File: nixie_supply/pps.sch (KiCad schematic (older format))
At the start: 5 parts

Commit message: minor cleanups
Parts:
- gave numbers to parts that had none: 3
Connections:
- net +5V: now also U5.2 (Enable); no longer U5.10 (Enable)
- net CLK_OUT: now also U5.14 (Q4); no longer U5.6 (Q4)
- net GND: now also U5.15 (Reset), U5.9 (CK); no longer U5.1 (CK), U5.7 (Reset)
- net at U4.6: now also U5.1 (CK); no longer U5.9 (CK)
- new net: U5.4 (Q2), U6.1
- new net: U5.10 (Enable), U5.5 (Q3), U6.2
- new net: U5.7 (Reset), U6.4
- new net: U6.3, U6.5, U6.6
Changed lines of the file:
@@
 $EndDescr
 $Comp
-L LM741 U?
+L LM741 U4
 U 1 1 5910E51A
 P 3200 2400
-F 0 "U?" H 3200 2650 50  0000 L CNN
+F 0 "U4" H 3200 2650 50  0000 L CNN
 F 1 "LM741" H 3200 2550 50  0000 L CNN
 F 2 "" H 3250 2450 50  0000 C CNN
@@
 $EndComp
 $Comp
-L 4518 U?
-U 2 1 5910E65E
+L 4518 U5
+U 1 1 5910E65E
 P 4650 2500
-F 0 "U?" H 4700 2950 50  0000 C CNN
+F 0 "U5" H 4700 2950 50  0000 C CNN
 F 1 "4518" H 4850 2150 50  0000 C CNN
 F 2 "" H 4650 2500 60  0001 C CNN
 F 3 "" H 4650 2500 60  0001 C CNN
-	2    4650 2500
-	1    0    0    -1
-$EndComp
-$Comp
-L 4518 U?
-U 1 1 5910E681
+	1    4650 2500
+	1    0    0    -1
+$EndComp
+$Comp
+L 4518 U5
+U 2 1 5910E681
 P 4650 4250
-F 0 "U?" H 4700 4700 50  0000 C CNN
+F 0 "U5" H 4700 4700 50  0000 C CNN
 F 1 "4518" H 4850 3900 50  0000 C CNN
 F 2 "" H 4650 4250 60  0001 C CNN
 F 3 "" H 4650 4250 60  0001 C CNN
-	1    4650 4250
-	1    0    0    -1
-$EndComp
-$Comp
-L 4011 U?
-U 4 1 5910E75D
+	2    4650 4250
+	1    0    0    -1
+$EndComp
+$Comp
+L 4011 U6
+U 1 1 5910E75D
 P 6200 2600
-F 0 "U?" H 6200 2650 50  0000 C CNN
+F 0 "U6" H 6200 2650 50  0000 C CNN
 F 1 "4011" H 6200 2550 50  0000 C CNN
 F 2 "" H 6200 2600 60  0001 C CNN
 F 3 "" H 6200 2600 60  0001 C CNN
-	4    6200 2600
-	1    0    0    -1
-$EndComp
-$Comp
-L 4011 U?
-U 1 1 5910E790
+	1    6200 2600
+	1    0    0    -1
+$EndComp
+$Comp
+L 4011 U6
+U 2 1 5910E790
 P 6200 3200
-F 0 "U?" H 6200 3250 50  0000 C CNN
+F 0 "U6" H 6200 3250 50  0000 C CNN
 F 1 "4011" H 6200 3150 50  0000 C CNN
 F 2 "" H 6200 3200 60  0001 C CNN
 F 3 "" H 6200 3200 60  0001 C CNN
-	1    6200 3200
+	2    6200 3200
 	1    0    0    -1
 $EndComp
@@
 NoConn ~ 5250 4100
 $Comp
-L +5V #PWR?
+L +5V #PWR035
 U 1 1 5910F1F9
 P 4050 2200
-F 0 "#PWR?" H 4050 2050 50  0001 C CNN
+F 0 "#PWR035" H 4050 2050 50  0001 C CNN
 F 1 "+5V" H 4050 2340 50  0000 C CNN
 F 2 "" H 4050 2200 50  0000 C CNN
@@
 $EndComp
 $Comp
-L +5V #PWR?
+L +5V #PWR036
 U 1 1 5910F217
 P 3100 2000
-F 0 "#PWR?" H 3100 1850 50  0001 C CNN
+F 0 "#PWR036" H 3100 1850 50  0001 C CNN
 F 1 "+5V" H 3100 2140 50  0000 C CNN
 F 2 "" H 3100 2000 50  0000 C CNN
@@
 $EndComp
 $Comp
-L GND #PWR?
+L GND #PWR037
 U 1 1 5910F235
 P 3100 2800
-F 0 "#PWR?" H 3100 2550 50  0001 C CNN
+F 0 "#PWR037" H 3100 2550 50  0001 C CNN
 F 1 "GND" H 3100 2650 50  0000 C CNN
 F 2 "" H 3100 2800 50  0000 C CNN
@@
 $EndComp
 $Comp
-L GND #PWR?
+L GND #PWR038
 U 1 1 5910F253
 P 3950 4400
-F 0 "#PWR?" H 3950 4150 50  0001 C CNN
+F 0 "#PWR038" H 3950 4150 50  0001 C CNN
 F 1 "GND" H 3950 4250 50  0000 C CNN
 F 2 "" H 3950 4400 50  0000 C CNN
@@
 Connection ~ 3950 4200
 $Comp
-L +5V #PWR?
+L +5V #PWR039
 U 1 1 5910F865
 P 2300 3300
-F 0 "#PWR?" H 2300 3150 50  0001 C CNN
+F 0 "#PWR039" H 2300 3150 50  0001 C CNN
 F 1 "+5V" H 2300 3440 50  0000 C CNN
 F 2 "" H 2300 3300 50  0000 C CNN
@@
 $EndComp
 $Comp
-L GND #PWR?
+L GND #PWR040
 U 1 1 5910F883
 P 2300 3600
-F 0 "#PWR?" H 2300 3350 50  0001 C CNN
+F 0 "#PWR040" H 2300 3350 50  0001 C CNN
 F 1 "GND" H 2300 3450 50  0000 C CNN
 F 2 "" H 2300 3600 50  0000 C CNN
@@
 $EndComp
 $Comp
-L VDD #PWR?
+L VDD #PWR041
 U 1 1 5910F8A1
 P 2550 3300
-F 0 "#PWR?" H 2550 3150 50  0001 C CNN
+F 0 "#PWR041" H 2550 3150 50  0001 C CNN
 F 1 "VDD" H 2550 3450 50  0000 C CNN
 F 2 "" H 2550 3300 50  0000 C CNN
@@
 $EndComp
 $Comp
-L VSS #PWR?
+L VSS #PWR042
 U 1 1 5910F8BF
 P 2550 3600
-F 0 "#PWR?" H 2550 3450 50  0001 C CNN
+F 0 "#PWR042" H 2550 3450 50  0001 C CNN
 F 1 "VSS" H 2550 3750 50  0000 C CNN
 F 2 "" H 2550 3600 50  0000 C CNN

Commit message: Footprint associations
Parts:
- U4: footprint (none) -> Housings_DIP:DIP-8_W7.62mm
- U5: footprint (none) -> Housings_DIP:DIP-16_W7.62mm
- U6: footprint (none) -> Housings_DIP:DIP-14_W7.62mm
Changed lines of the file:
@@
 F 0 "U4" H 3200 2650 50  0000 L CNN
 F 1 "LM741" H 3200 2550 50  0000 L CNN
-F 2 "" H 3250 2450 50  0000 C CNN
+F 2 "Housings_DIP:DIP-8_W7.62mm" H 3250 2450 50  0001 C CNN
 F 3 "" H 3350 2550 50  0000 C CNN
 	1    3200 2400
@@
 F 0 "U5" H 4700 2950 50  0000 C CNN
 F 1 "4518" H 4850 2150 50  0000 C CNN
-F 2 "" H 4650 2500 60  0001 C CNN
+F 2 "Housings_DIP:DIP-16_W7.62mm" H 4650 2500 60  0001 C CNN
 F 3 "" H 4650 2500 60  0001 C CNN
 	1    4650 2500
@@
 F 0 "U5" H 4700 4700 50  0000 C CNN
 F 1 "4518" H 4850 3900 50  0000 C CNN
-F 2 "" H 4650 4250 60  0001 C CNN
+F 2 "Housings_DIP:DIP-16_W7.62mm" H 4650 4250 60  0001 C CNN
 F 3 "" H 4650 4250 60  0001 C CNN
 	2    4650 4250
@@
 F 0 "U6" H 6200 2650 50  0000 C CNN
 F 1 "4011" H 6200 2550 50  0000 C CNN
-F 2 "" H 6200 2600 60  0001 C CNN
+F 2 "Housings_DIP:DIP-14_W7.62mm" H 6200 2600 60  0001 C CNN
 F 3 "" H 6200 2600 60  0001 C CNN
 	1    6200 2600
@@
 F 0 "U6" H 6200 3250 50  0000 C CNN
 F 1 "4011" H 6200 3150 50  0000 C CNN
-F 2 "" H 6200 3200 60  0001 C CNN
+F 2 "Housings_DIP:DIP-14_W7.62mm" H 6200 3200 60  0001 C CNN
 F 3 "" H 6200 3200 60  0001 C CNN
 	2    6200 3200

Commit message: Clock board layout
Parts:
- U4: symbol LM741 -> LM741-RESCUE-nixie_supply
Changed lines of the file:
@@
 EESchema Schematic File Version 2
+LIBS:nixie_supply-rescue
 LIBS:power
 LIBS:device
@@
 $EndDescr
 $Comp
-L LM741 U4
+L LM741-RESCUE-nixie_supply U4
 U 1 1 5910E51A
 P 3200 2400

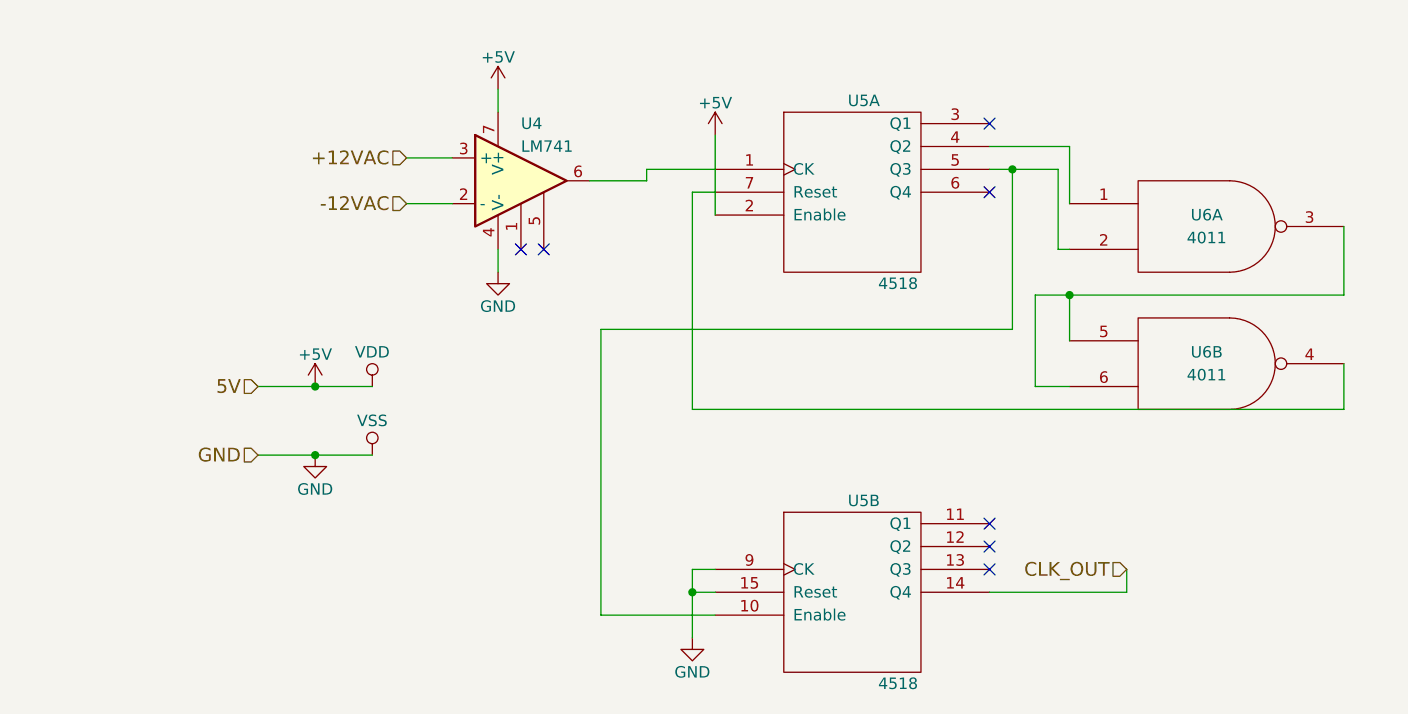
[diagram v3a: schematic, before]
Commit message: Supply board mk2: reduced time base noise, upped some clearances, added ground plane
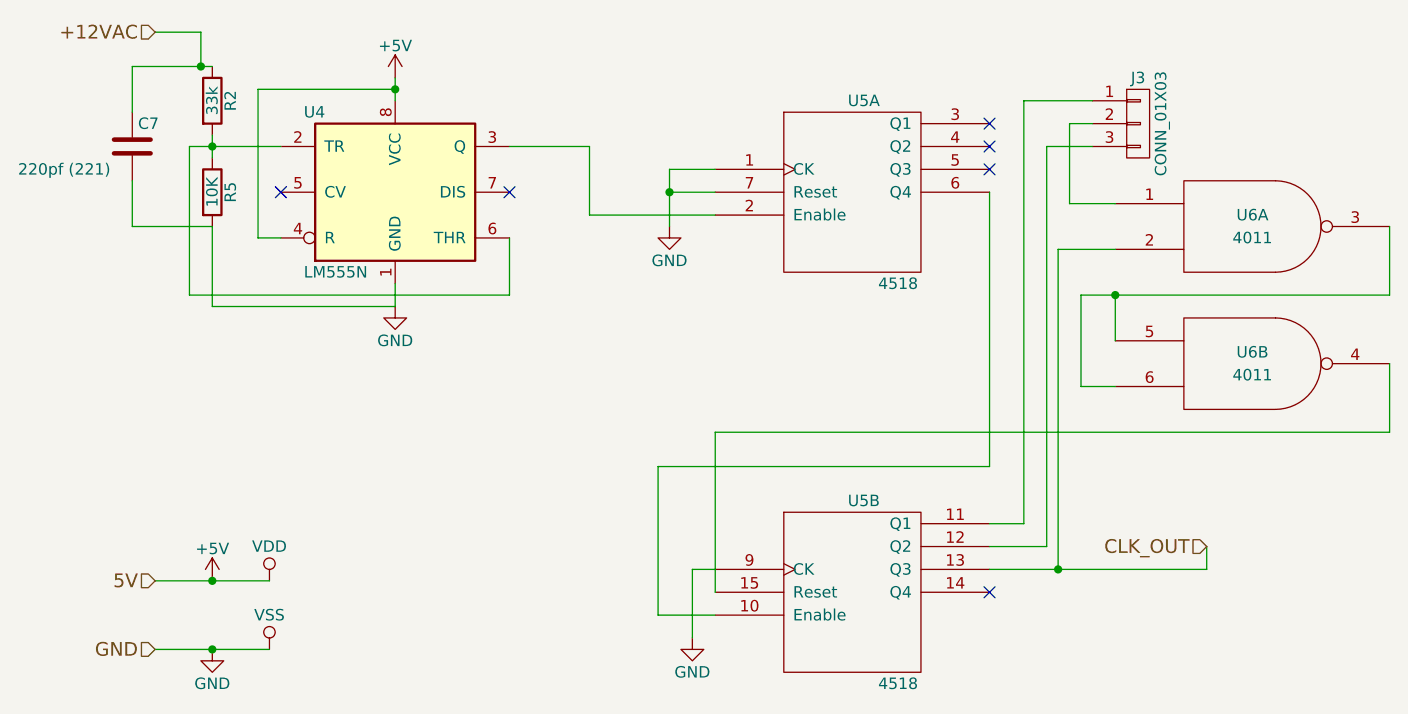
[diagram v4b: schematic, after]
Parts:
- removed U4: LM741, Housings_DIP:DIP-8_W7.62mm, symbol LM741-RESCUE-nixie_supply
- added C7: 220pf (221), Capacitors_THT:C_Disc_D10.0mm_W2.5mm_P5.00mm, symbol C
- added J3: CONN_01X03, Pin_Headers:Pin_Header_Straight_1x03_Pitch2.54mm, symbol CONN_01X03
- added R2: 33k, Resistors_THT:R_Axial_DIN0207_L6.3mm_D2.5mm_P10.16mm_Horizontal, symbol R
- added R5: 10K, Resistors_THT:R_Axial_DIN0207_L6.3mm_D2.5mm_P10.16mm_Horizontal, symbol R
- added U4: LM555N, Housings_DIP:DIP-8_W7.62mm, symbol LM555N
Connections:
- net +12VAC: now also C7.1, R2.1
- net +5V: now also U4.4 (R), U4.8 (VCC); no longer U5.2 (Enable)
- net CLK_OUT: now also U5.13 (Q3), U6.2; no longer U5.14 (Q4)
- net GND: now also U5.1 (CK), U5.7 (Reset), C7.2, R5.2, U4.1 (GND); no longer U5.15 (Reset)
- net at U5.4 (Q2): no longer U6.1
- net at U5.6 (Q4): now also U5.10 (Enable)
- net at U6.4: now also U5.15 (Reset); no longer U5.7 (Reset)
- net at U5.11 (Q1): now also J3.1 (P1)
- net at U5.12 (Q2): now also J3.3 (P3)
- new net: U4.3 (Q), U5.2 (Enable)
- new net: J3.2 (P2), U6.1
- new net: R2.2, R5.1, U4.2 (TR), U4.6 (THR)
- now unconnected: U5.5 (Q3)
- no-connect marks 7 -> 6
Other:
- moved on the sheet: U6A, U6B

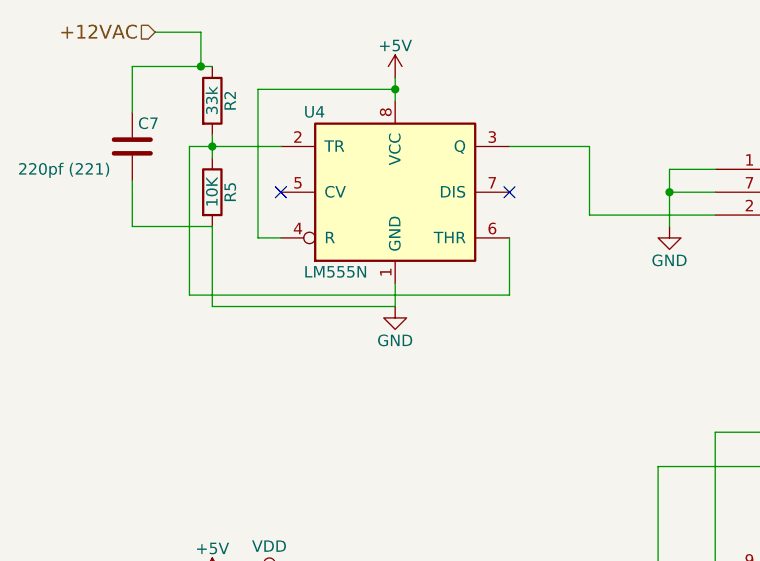
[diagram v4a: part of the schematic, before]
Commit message: Added more noise reduction to clock signal, added top ground plane
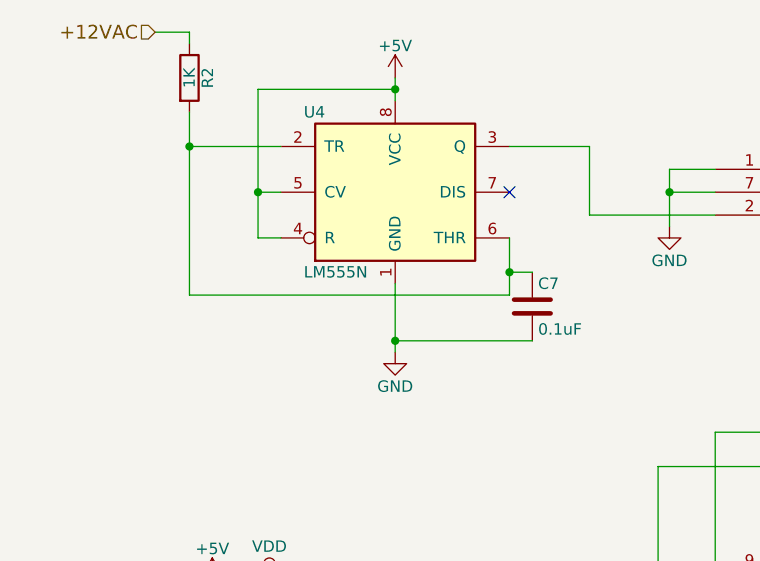
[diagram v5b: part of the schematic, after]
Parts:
- removed R5: 10K, Resistors_THT:R_Axial_DIN0207_L6.3mm_D2.5mm_P10.16mm_Horizontal, symbol R
- C7: value 220pf (221) -> 0.1uF; footprint Capacitors_THT:C_Disc_D10.0mm_W2.5mm_P5.00mm -> (none)
- R2: value 33k -> 1K; footprint Resistors_THT:R_Axial_DIN0207_L6.3mm_D2.5mm_P10.16mm_Horizontal -> (none)
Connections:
- net +12VAC: no longer C7.1
- net +5V: now also U4.5 (CV)
- net at R2.2, U4.2 (TR), U4.6 (THR): now also C7.1
- no-connect marks 6 -> 5
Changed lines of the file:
@@
 CLK_OUT
 Connection ~ 1850 4150
-Wire Wire Line
-	1600 1750 1800 1750
 Text HLabel 1600 4450 0    60   Input ~ 0
 GND
@@
 L GND #PWR040
 U 1 1 59851A7B
-P 2650 2950
-F 0 "#PWR040" H 2650 2700 50  0001 C CNN
-F 1 "GND" H 2650 2800 50  0000 C CNN
-F 2 "" H 2650 2950 50  0001 C CNN
-F 3 "" H 2650 2950 50  0001 C CNN
-	1    2650 2950
-	1    0    0    -1
-$EndComp
-$Comp
-L R R2
-U 1 1 59851ABC
-P 1850 2050
-F 0 "R2" V 1930 2050 50  0000 C CNN
-F 1 "33k" V 1850 2050 50  0000 C CNN
-F 2 "Resistors_THT:R_Axial_DIN0207_L6.3mm_D2.5mm_P10.16mm_Horizontal" V 1780 2050 50  0001 C CNN
-F 3 "" H 1850 2050 50  0001 C CNN
-	1    1850 2050
-	1    0    0    -1
-$EndComp
-$Comp
-L R R5
-U 1 1 59851B3F
-P 1850 2450
-F 0 "R5" V 1930 2450 50  0000 C CNN
-F 1 "10K" V 1850 2450 50  0000 C CNN
-F 2 "Resistors_THT:R_Axial_DIN0207_L6.3mm_D2.5mm_P10.16mm_Horizontal" V 1780 2450 50  0001 C CNN
-F 3 "" H 1850 2450 50  0001 C CNN
-	1    1850 2450
-	1    0    0    -1
-$EndComp
-$Comp
-L C C7
-U 1 1 59851B6E
-P 1500 2250
-F 0 "C7" H 1525 2350 50  0000 L CNN
-F 1 "220pf (221)" H 1000 2150 50  0000 L CNN
-F 2 "Capacitors_THT:C_Disc_D10.0mm_W2.5mm_P5.00mm" H 1538 2100 50  0001 C CNN
-F 3 "" H 1500 2250 50  0001 C CNN
-	1    1500 2250
+P 2650 3150
+F 0 "#PWR040" H 2650 2900 50  0001 C CNN
+F 1 "GND" H 2650 3000 50  0000 C CNN
+F 2 "" H 2650 3150 50  0001 C CNN
+F 3 "" H 2650 3150 50  0001 C CNN
+	1    2650 3150
 	1    0    0    -1
 $EndComp
@@
 $EndComp
 Wire Wire Line
-	1500 2100 1500 1900
-Wire Wire Line
-	1500 1900 1850 1900
-Wire Wire Line
-	1850 2200 1850 2300
-Wire Wire Line
-	1850 2600 1500 2600
-Wire Wire Line
-	1500 2600 1500 2400
-Wire Wire Line
-	1850 2600 1850 2950
-Wire Wire Line
-	1850 2950 2650 2950
-Wire Wire Line
-	2650 2950 2650 2850
-Wire Wire Line
 	2650 2050 2650 1950
 Wire Wire Line
@@
 Wire Wire Line
 	1750 2250 2150 2250
-Connection ~ 1850 2250
-Wire Wire Line
-	1800 1750 1800 1900
-Connection ~ 1800 1900
 Wire Wire Line
 	3150 2650 3150 2900
-NoConn ~ 2150 2450
 NoConn ~ 3150 2450
 Wire Wire Line
@@
 	3150 2900 1750 2900
 Wire Wire Line
-	1750 2900 1750 2250
+	1750 2900 1750 2100
 $Comp
 L 4011 U6
@@
 Wire Wire Line
 	5600 2150 5700 2150
+Wire Wire Line
+	2150 2450 2050 2450
+Connection ~ 2050 2450
+$Comp
+L R R2
+U 1 1 59875D14
+P 1750 1950
+F 0 "R2" V 1830 1950 50  0000 C CNN
+F 1 "1K" V 1750 1950 50  0000 C CNN
+F 2 "" V 1680 1950 50  0001 C CNN
+F 3 "" H 1750 1950 50  0001 C CNN
+	1    1750 1950
+	1    0    0    -1
+$EndComp
+Wire Wire Line
+	1600 1750 1750 1750
+Wire Wire Line
+	1750 1750 1750 1800
+Connection ~ 1750 2250
+Wire Wire Line
+	2650 2850 2650 3150
+$Comp
+L C C7
+U 1 1 59875E63
+P 3250 2950
+F 0 "C7" H 3275 3050 50  0000 L CNN
+F 1 "0.1uF" H 3275 2850 50  0000 L CNN
+F 2 "" H 3288 2800 50  0001 C CNN
+F 3 "" H 3250 2950 50  0001 C CNN
+	1    3250 2950
+	1    0    0    -1
+$EndComp
+Wire Wire Line
+	3250 2800 3150 2800
+Connection ~ 3150 2800
+Wire Wire Line
+	3250 3100 2650 3100
+Connection ~ 2650 3100
 $EndSCHEMATC
